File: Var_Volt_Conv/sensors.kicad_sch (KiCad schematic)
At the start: 6 parts

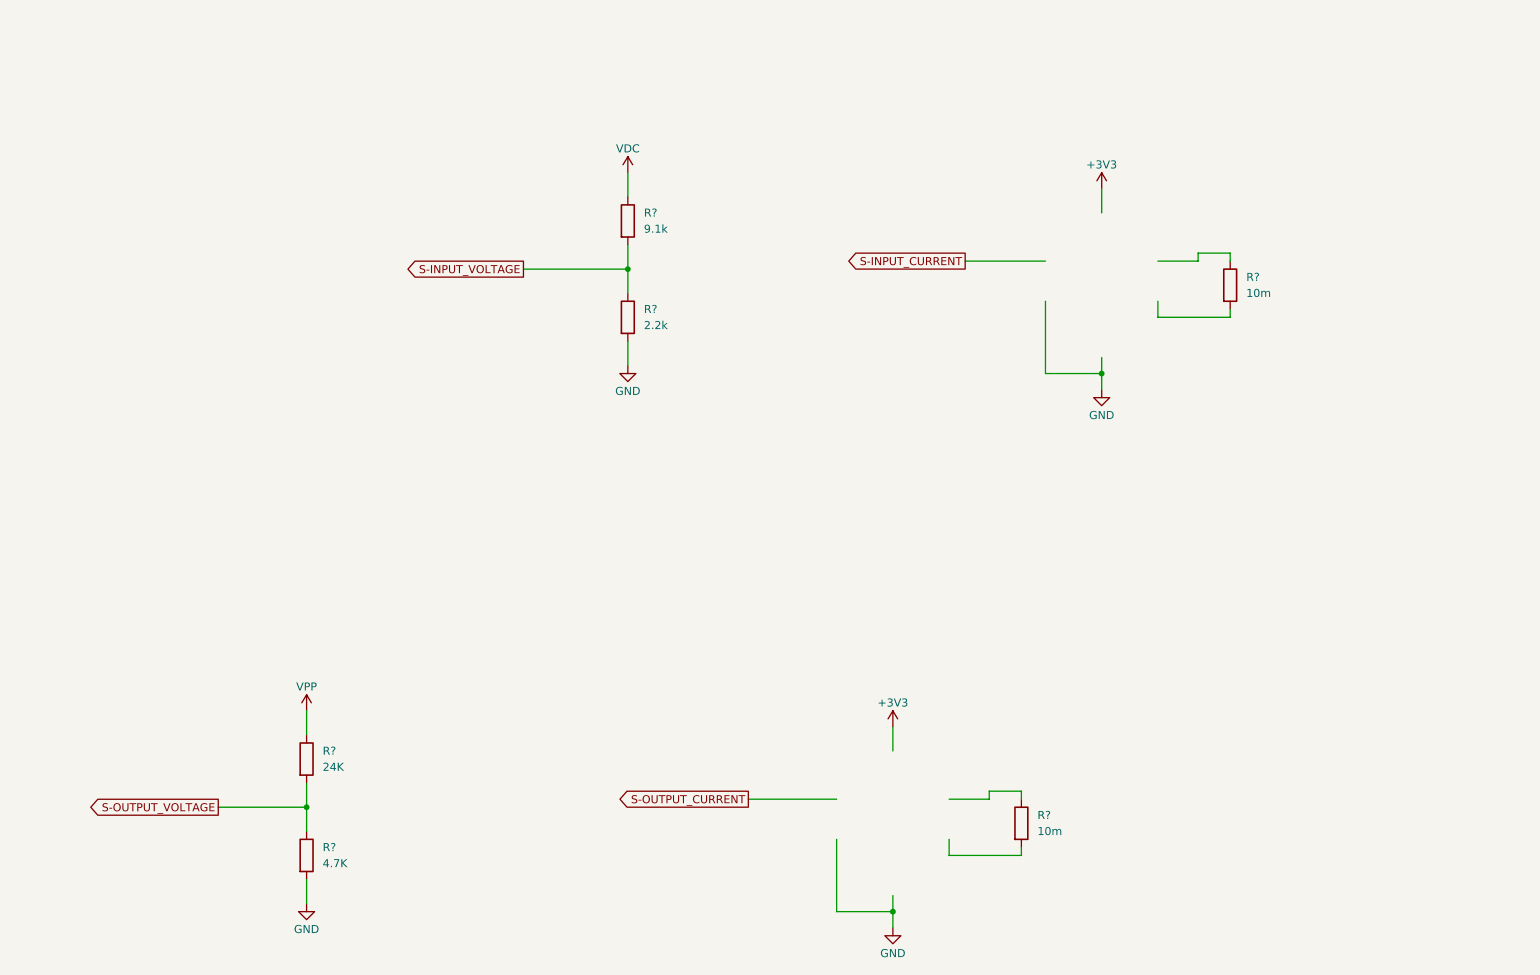
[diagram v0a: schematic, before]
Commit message: Complete Sensors Schematic
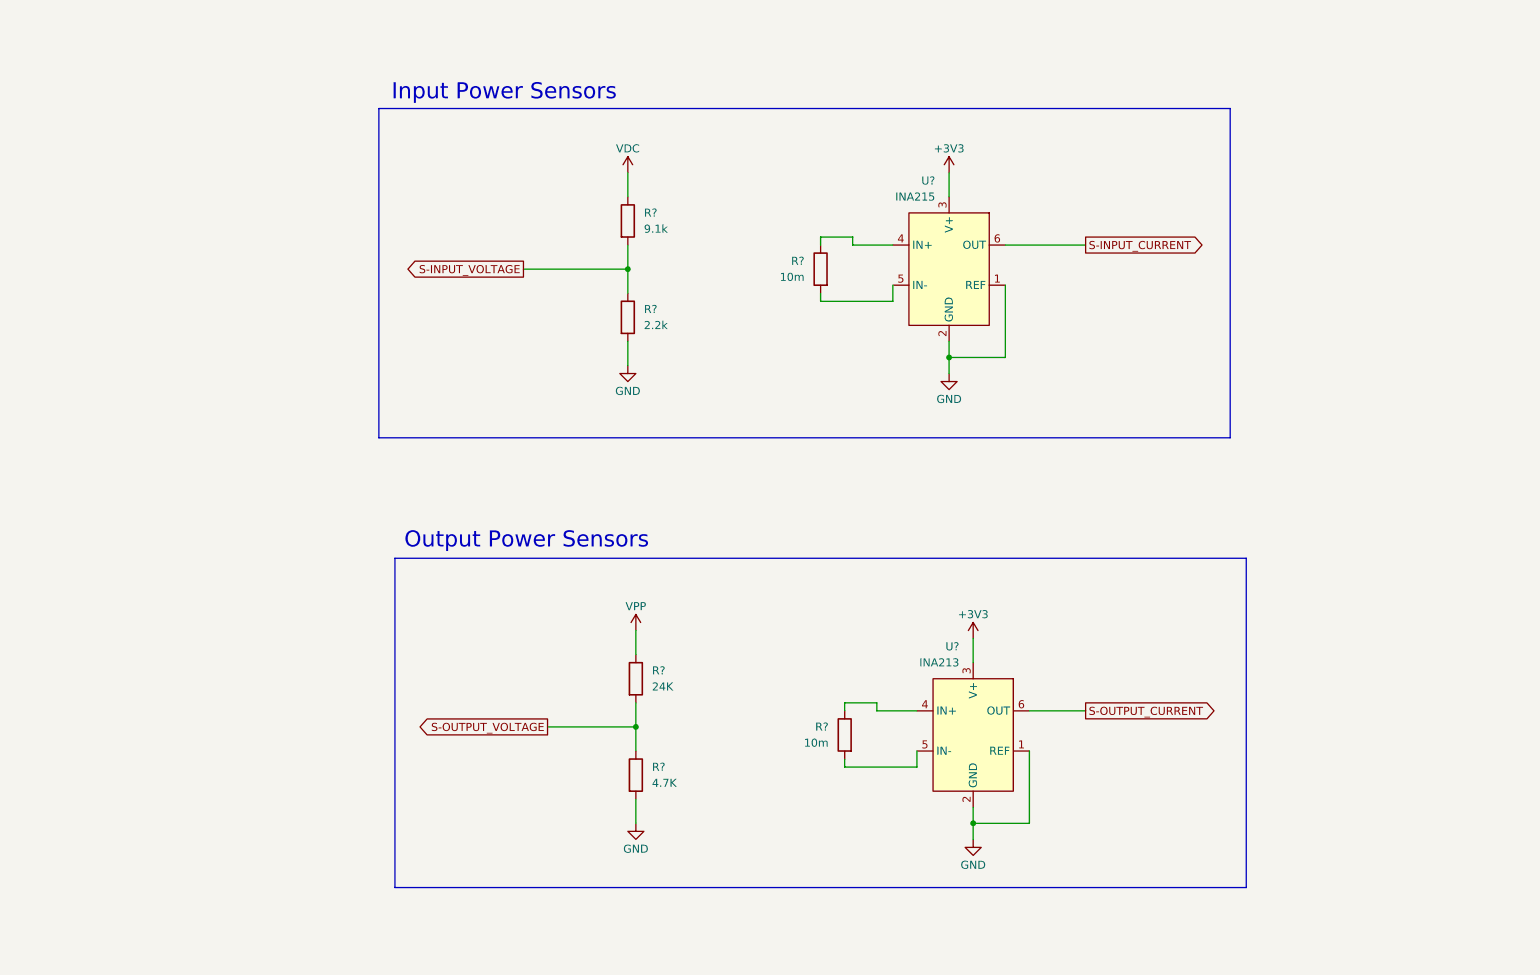
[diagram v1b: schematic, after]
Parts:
- added U?: INA213, symbol INA21x Current-Shunt Monitors:INA213
- added U?: INA215, symbol INA21x Current-Shunt Monitors:INA215
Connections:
- net +3V3: now also U?.3 (V+), U?.3 (V+)
- net GND: now also U?.1 (REF), U?.1 (REF), U?.2 (GND), U?.2 (GND)
- net S-INPUT_CURRENT: now also U?.6 (OUT)
- net S-OUTPUT_CURRENT: now also U?.6 (OUT)
- net at R?.1: now also U?.4 (IN+) (x2)
- net at R?.2: now also U?.5 (IN-) (x2)
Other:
- note added: "Input Power Sensors"
- note added: "Output Power Sensors"
- moved on the sheet: R?

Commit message: Add bounding boxes and title/labels to all the sub-circuits
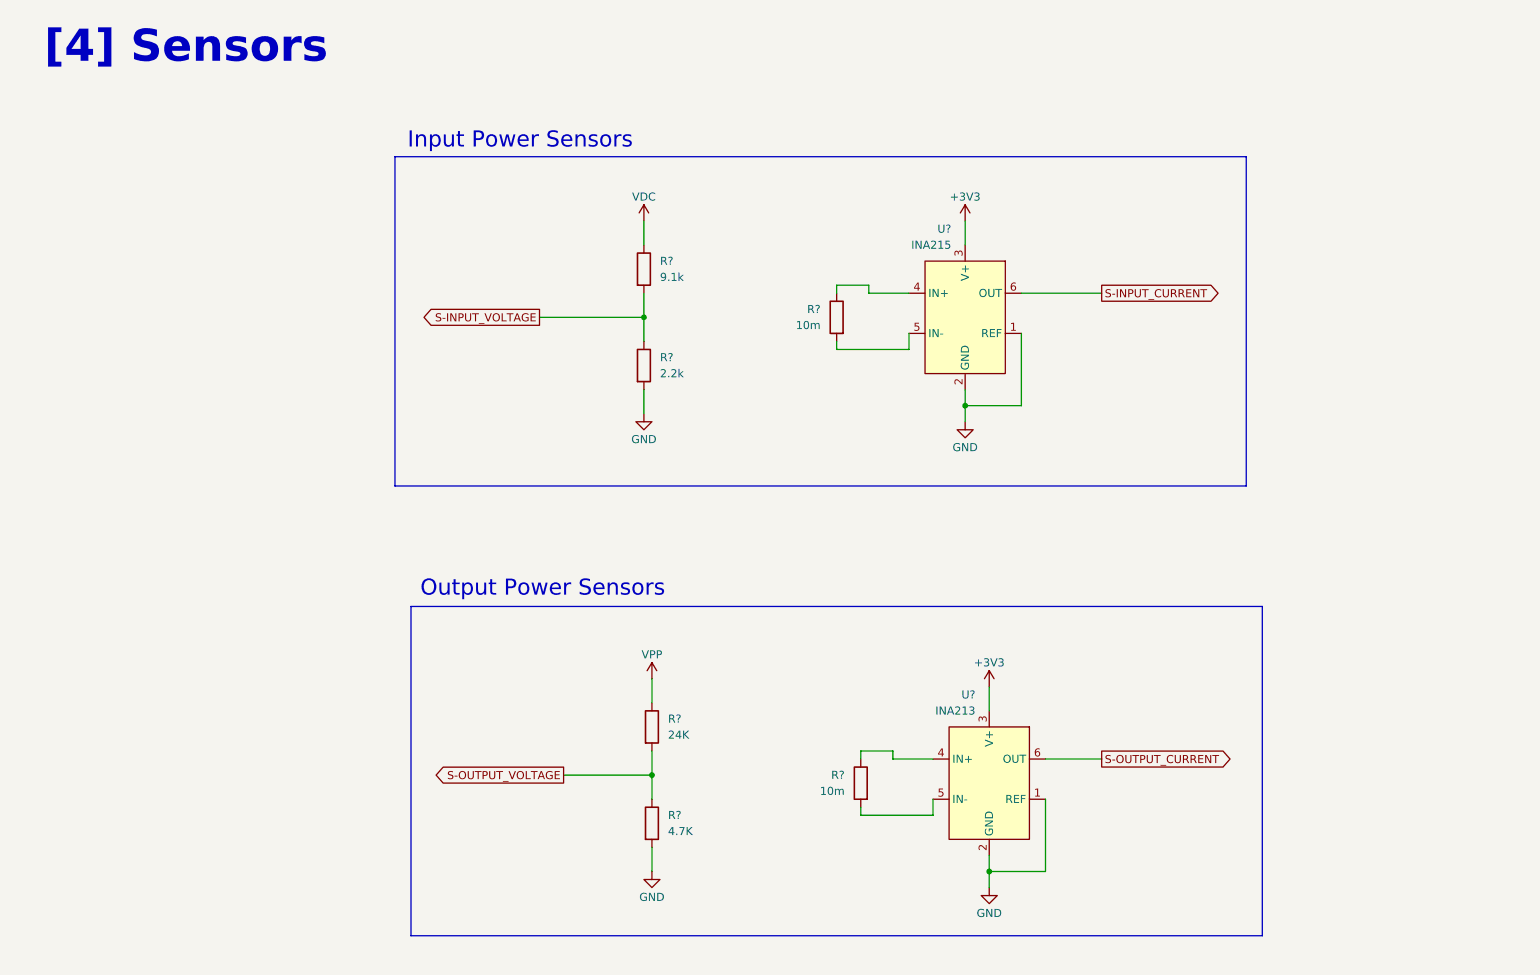
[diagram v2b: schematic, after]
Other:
- note added: "[4] Sensors"
- moved on the sheet: R?, U?

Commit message: Rename power nets and integrated current sensing into power circuit
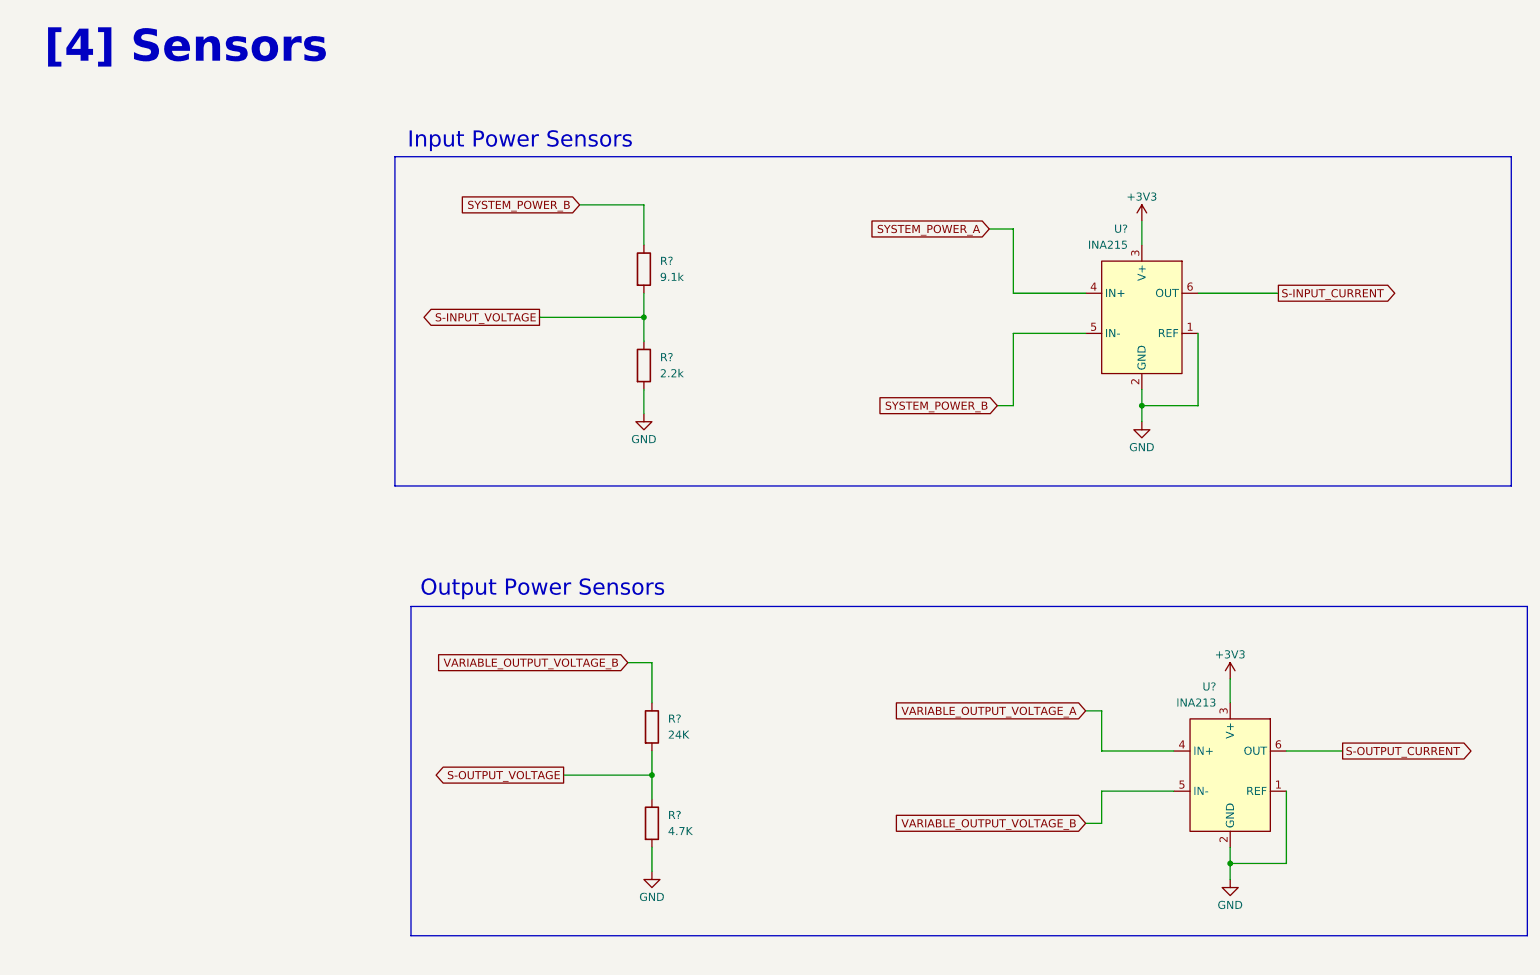
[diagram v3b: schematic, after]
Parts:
- removed R? (x2): 10m, symbol Device:R
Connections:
- net VDC is gone; now on net SYSTEM_POWER_B: R?.1
- net VPP is gone; now on net VARIABLE_OUTPUT_VOLTAGE_B: R?.1
- net VARIABLE_OUTPUT_VOLTAGE_A: now reaches U?.4 (IN+)
- net VARIABLE_OUTPUT_VOLTAGE_B: now reaches U?.5 (IN-)
- net SYSTEM_POWER_A: now reaches U?.4 (IN+)
- net SYSTEM_POWER_B: now reaches U?.5 (IN-)
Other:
- moved on the sheet: U?

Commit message: Finalized current sensing circuit values
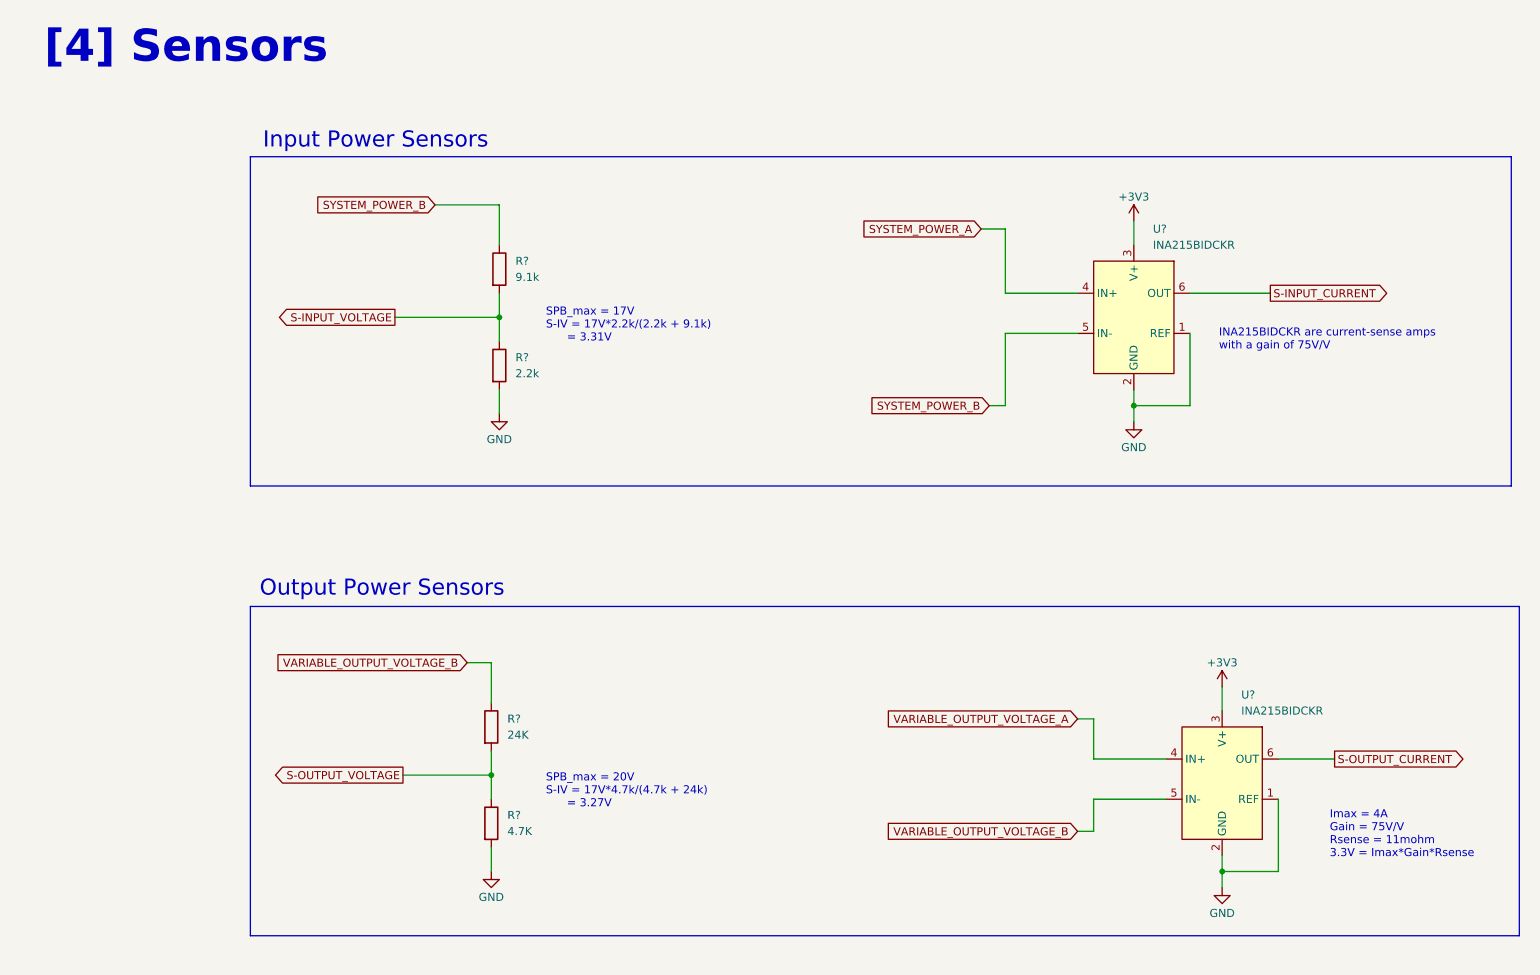
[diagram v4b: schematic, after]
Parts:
- removed U?: INA213, symbol INA21x Current-Shunt Monitors:INA213
- added U?: INA215BIDCKR, symbol INA21x Current-Shunt Monitors:INA215
- U?: value INA215 -> INA215BIDCKR
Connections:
- net +3V3: now also U?.3 (V+)
- net GND: now also U?.1 (REF), U?.2 (GND)
- net S-OUTPUT_CURRENT: now also U?.6 (OUT)
- net VARIABLE_OUTPUT_VOLTAGE_A: now also U?.4 (IN+)
- net VARIABLE_OUTPUT_VOLTAGE_B: now also U?.5 (IN-)
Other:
- note added: "INA215BIDCKR are current-sense amps with a gain of 75V/V"
- note added: "Imax = 4A Gain = 75V/V Rsense = 11mohm 3.3V = Imax*Gain*Rsense"
- note added: "SPB_max = 17V S-IV = 17V*2.2k/(2.2k + 9.1k) = 3.31V"
- note added: "SPB_max = 20V S-IV = 17V*4.7k/(4.7k + 24k) = 3.27V"
- moved on the sheet: R?, U?

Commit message: Annotated schematic symbols
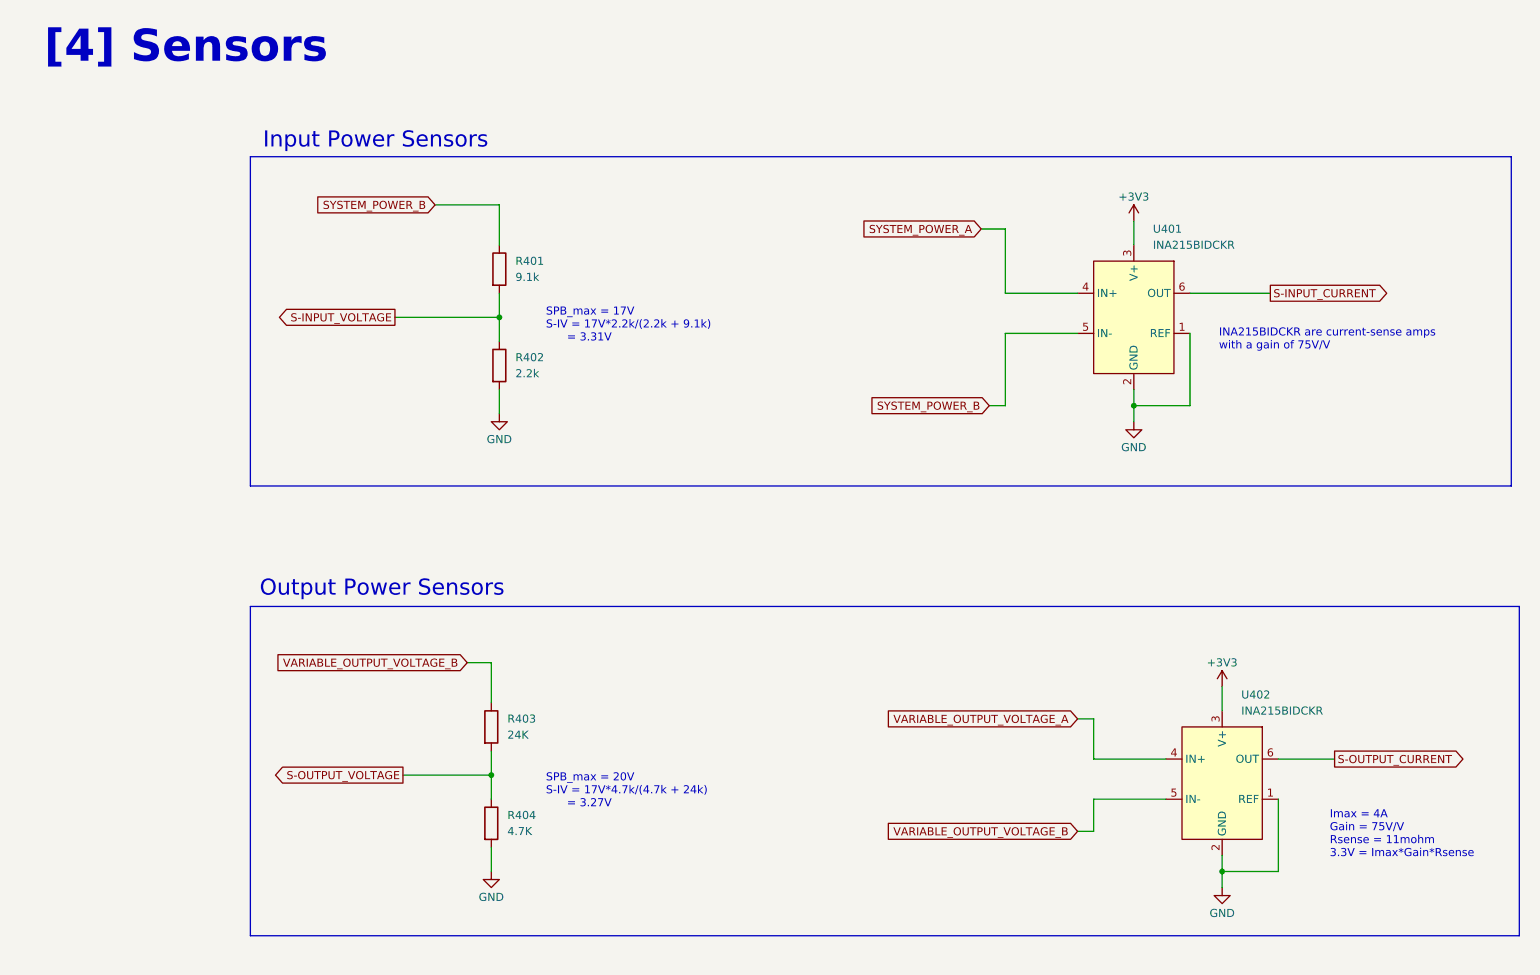
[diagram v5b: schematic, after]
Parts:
- gave numbers to parts that had none: 6
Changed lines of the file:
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@@
 		(dnp no)
 		(fields_autoplaced yes)
-		(property "Reference" "U?"
+		(property "Reference" "U402"
 			(at 206.2165 124.46 0)
 			(effects
@@
 			(project "Var_Volt_Conv"
 				(path "/7c9580d6-c22f-4506-b9c3-9272e882c9fb/a939aa62-b331-46a3-b3e0-48fa29856a0e"
-					(reference "U?")
+					(reference "U402")
 					(unit 1)
 				)
@@
 		(dnp no)
 		(fields_autoplaced yes)
-		(property "Reference" "R?"
+		(property "Reference" "R403"
 			(at 90.17 128.2699 0)
 			(effects
@@
 			(project "Var_Volt_Conv"
 				(path "/7c9580d6-c22f-4506-b9c3-9272e882c9fb/a939aa62-b331-46a3-b3e0-48fa29856a0e"
-					(reference "R?")
+					(reference "R403")
 					(unit 1)
 				)
@@
 		(dnp no)
 		(fields_autoplaced yes)
-		(property "Reference" "R?"
+		(property "Reference" "R401"
 			(at 91.44 55.8799 0)
 			(effects
@@
 			(project ""
 				(path "/7c9580d6-c22f-4506-b9c3-9272e882c9fb/a939aa62-b331-46a3-b3e0-48fa29856a0e"
-					(reference "R?")
+					(reference "R401")
 					(unit 1)
 				)
@@
 		(dnp no)
 		(fields_autoplaced yes)
-		(property "Reference" "R?"
+		(property "Reference" "R404"
 			(at 90.17 143.5099 0)
 			(effects
@@
 			(project "Var_Volt_Conv"
 				(path "/7c9580d6-c22f-4506-b9c3-9272e882c9fb/a939aa62-b331-46a3-b3e0-48fa29856a0e"
-					(reference "R?")
+					(reference "R404")
 					(unit 1)
 				)
@@
 		(dnp no)
 		(fields_autoplaced yes)
-		(property "Reference" "R?"
+		(property "Reference" "R402"
 			(at 91.44 71.1199 0)
 			(effects
@@
 			(project "Var_Volt_Conv"
 				(path "/7c9580d6-c22f-4506-b9c3-9272e882c9fb/a939aa62-b331-46a3-b3e0-48fa29856a0e"
-					(reference "R?")
+					(reference "R402")
 					(unit 1)
 				)
@@
 		(dnp no)
 		(fields_autoplaced yes)
-		(property "Reference" "U?"
+		(property "Reference" "U401"
 			(at 192.2465 50.8 0)
 			(effects
@@
 			(project ""
 				(path "/7c9580d6-c22f-4506-b9c3-9272e882c9fb/a939aa62-b331-46a3-b3e0-48fa29856a0e"
-					(reference "U?")
-					(unit 1)
-				)
+					(reference "U401")
+					(unit 1)
+				)
